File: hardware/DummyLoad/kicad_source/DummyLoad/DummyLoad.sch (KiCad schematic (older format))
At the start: 53 parts, among them CN1 60312202114509, CN2 60312202114509

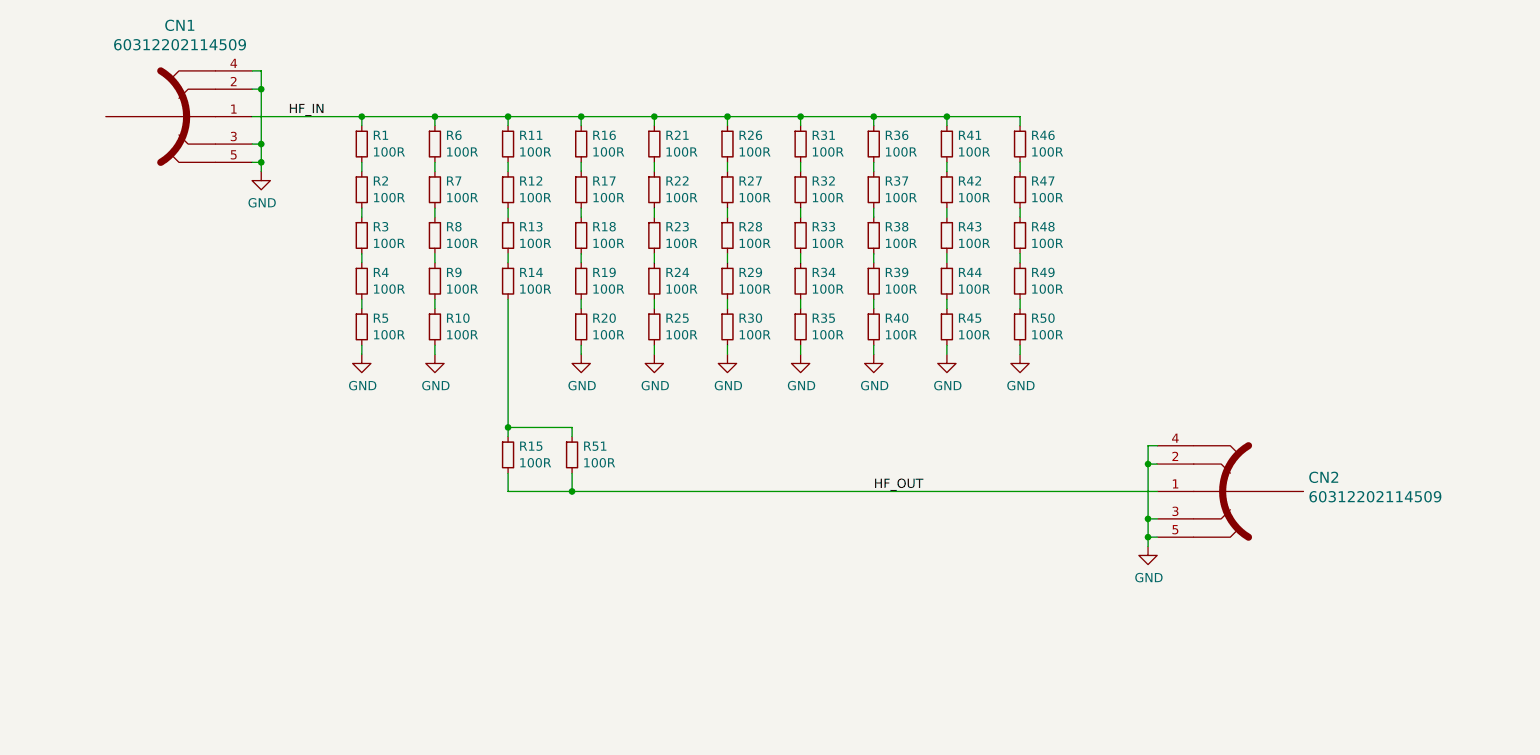
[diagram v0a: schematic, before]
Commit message: added comments to schematic, added laber with license to pcb
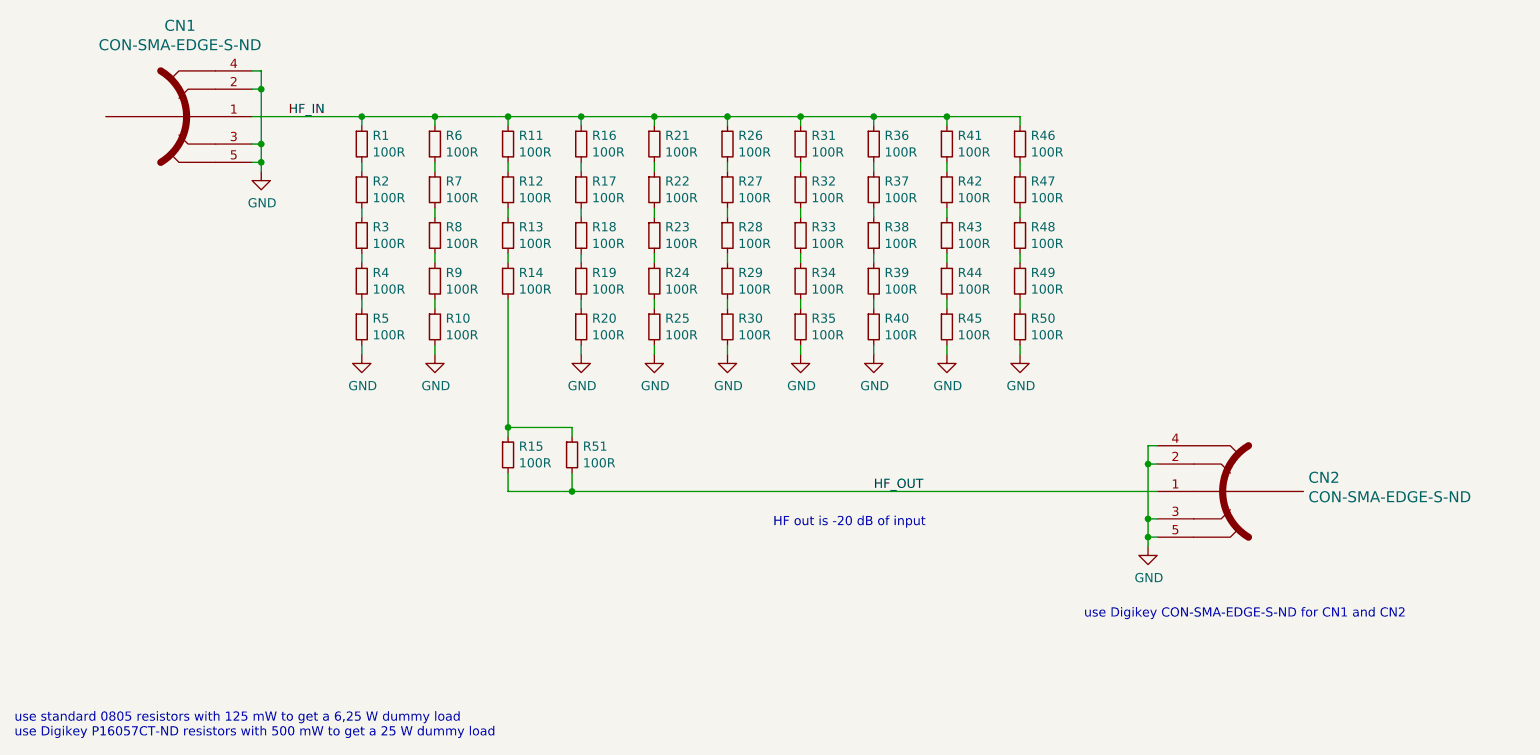
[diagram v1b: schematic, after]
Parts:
- CN1, CN2: value 60312202114509 -> CON-SMA-EDGE-S-ND
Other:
- note added: "HF out is -20 dB of input"
- note added: "use Digikey CON-SMA-EDGE-S-ND for CN1 and CN2"
- note added: "use standard 0805 resistors with 125 mW to get a 6,25 W dummy load\nuse Digikey P16057CT-ND resistors with 500 mW to get a 25 W dummy load"
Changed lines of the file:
@@
 EESchema Schematic File Version 4
+LIBS:DummyLoad-cache
 EELAYER 26 0
 EELAYER END
@@
 P 2600 2950
 F 0 "CN1" H 2406 3447 60  0000 C CNN
-F 1 "60312202114509" H 2406 3341 60  0000 C CNN
+F 1 "CON-SMA-EDGE-S-ND" H 2406 3341 60  0000 C CNN
 F 2 "CON_wuerth:WR-SMA-PCB" H 2406 3341 60  0001 C CNN
 F 3 "" H 2600 2950 60  0000 C CNN
@@
 P 7950 5000
 F 0 "CN2" H 7323 5075 60  0000 R CNN
-F 1 "60312202114509" H 7323 4969 60  0000 R CNN
+F 1 "CON-SMA-EDGE-S-ND" H 7323 4969 60  0000 R CNN
 F 2 "CON_wuerth:WR-SMA-PCB" H 7322 4969 60  0001 R CNN
 F 3 "" H 7950 5000 60  0000 C CNN
@@
 Wire Wire Line
 	4200 3750 4200 3700
+Text Notes 7350 5700 0    50   ~ 0
+use Digikey CON-SMA-EDGE-S-ND for CN1 and CN2
+Text Notes 5650 5200 0    50   ~ 0
+HF out is -20 dB of input
+Text Notes 1500 6350 0    50   ~ 0
+use standard 0805 resistors with 125 mW to get a 6,25 W dummy load\nuse Digikey P16057CT-ND resistors with 500 mW to get a 25 W dummy load
 $EndSCHEMATC
